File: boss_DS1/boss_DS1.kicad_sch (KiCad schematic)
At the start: 83 parts, among them J1 top_panel_connector, J2 Jack_6.35, J6 Jack_6.35, J7 Conn_01x01_Socket, J8 Conn_01x01_Socket, J9 Barrel_Jack_Switch, P1 boss_DS1_front_panel, P2 bottom_panel, Q1 MMBT5551, Q11 AO3401A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

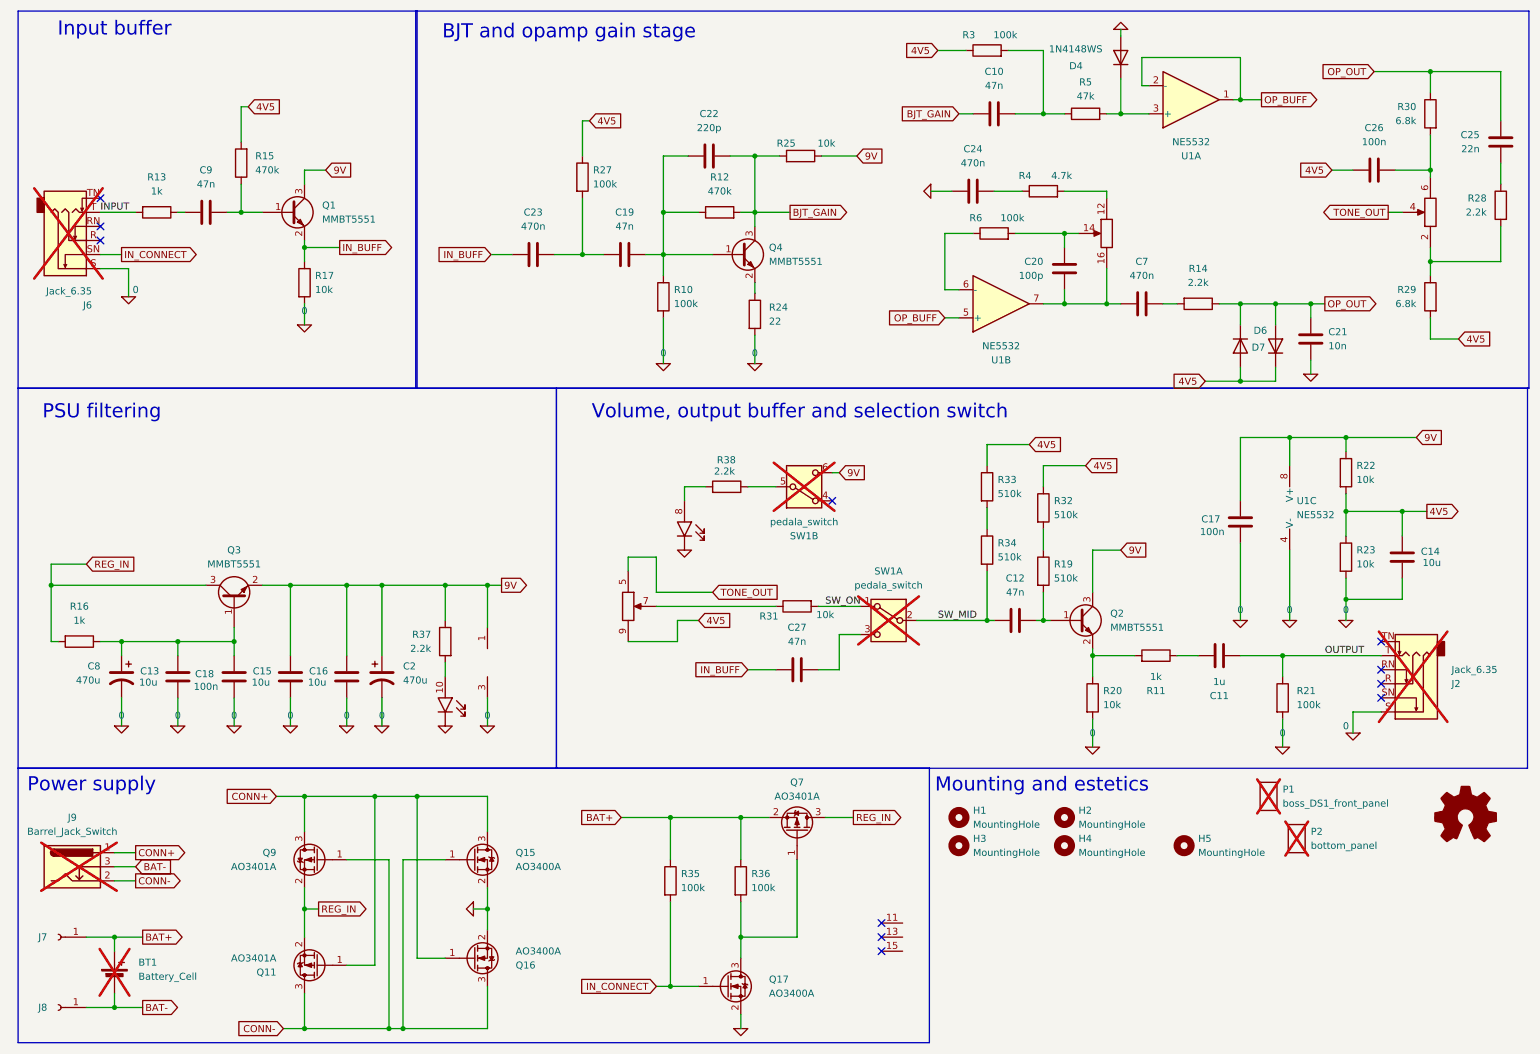
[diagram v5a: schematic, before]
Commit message: Front plate update, diodes rotated.
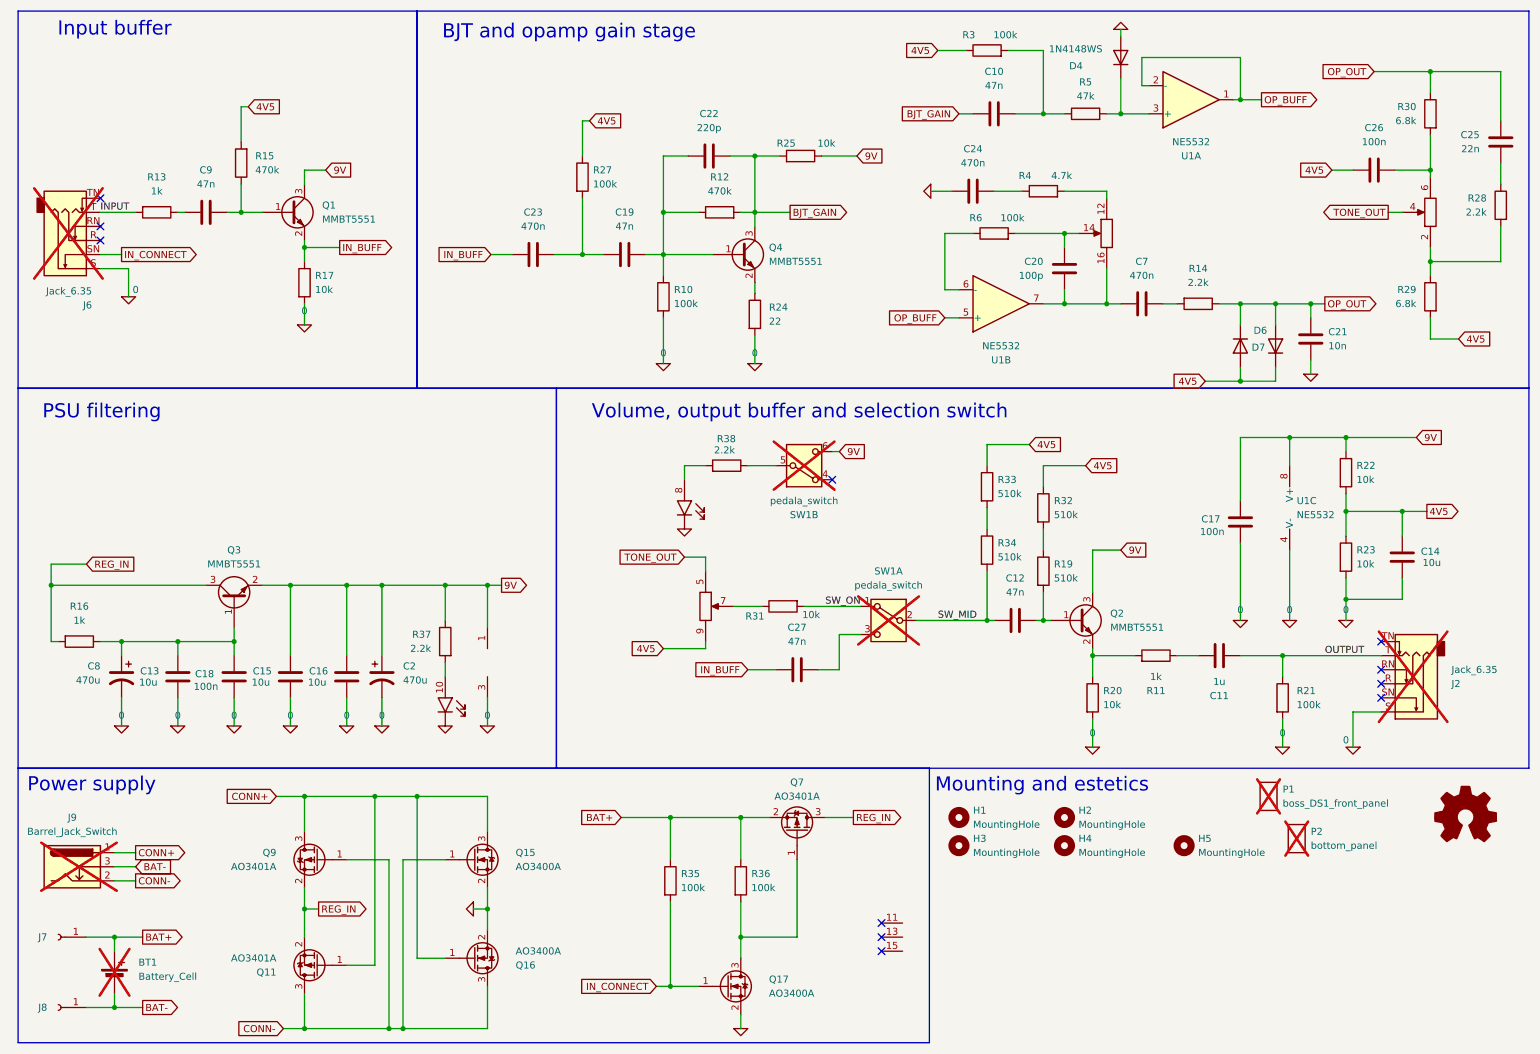
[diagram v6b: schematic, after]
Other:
- moved on the sheet: R31, R38, SW1B

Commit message: Updated all.
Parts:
- removed SIM1: Logo_Open_Hardware_Small, Symbol:OSHW-Logo2_7.3x6mm_SilkScreen, symbol Graphic:Logo_Open_Hardware_Small
- J1: footprint Connector_IDC:IDC-Header_2x08_P2.54mm_Vertical -> pedale:IDC-Header_2x08_P2.54mm_Vertical
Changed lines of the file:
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@@
 	)
 	(symbol
+		(lib_name "0_6")
 		(lib_id "Simulation_SPICE:0")
 		(at 50.8 140.97 0)
@@
 	)
 	(symbol
+		(lib_name "0_13")
 		(lib_id "Simulation_SPICE:0")
 		(at 232.41 121.92 0)
@@
 	)
 	(symbol
+		(lib_name "BC817_3")
 		(lib_id "Transistor_BJT:BC817")
 		(at 203.2 121.92 0)
@@
 	)
 	(symbol
+		(lib_name "0_12")
 		(lib_id "Simulation_SPICE:0")
 		(at 176.53 44.45 270)
@@
 			)
 		)
-		(property "Footprint" "Connector_IDC:IDC-Header_2x08_P2.54mm_Vertical"
+		(property "Footprint" "pedale:IDC-Header_2x08_P2.54mm_Vertical"
 			(at 96.52 135.89 0)
 			(effects
@@
 	)
 	(symbol
+		(lib_name "0_3")
 		(lib_id "Simulation_SPICE:0")
 		(at 210.82 15.24 0)
@@
 	)
 	(symbol
+		(lib_name "0_14")
 		(lib_id "Simulation_SPICE:0")
 		(at 40.64 140.97 0)
@@
 	)
 	(symbol
+		(lib_name "BC817_2")
 		(lib_id "Transistor_BJT:BC817")
 		(at 60.96 48.26 0)
@@
 			)
 		)
-		(property "Footprint" "Connector_IDC:IDC-Header_2x08_P2.54mm_Vertical"
+		(property "Footprint" "pedale:IDC-Header_2x08_P2.54mm_Vertical"
 			(at 266.7 48.26 0)
 			(effects
@@
 			)
 		)
-		(property "Footprint" "Connector_IDC:IDC-Header_2x08_P2.54mm_Vertical"
+		(property "Footprint" "pedale:IDC-Header_2x08_P2.54mm_Vertical"
 			(at 132.08 101.6 0)
 			(effects
@@
 			)
 		)
-		(property "Footprint" "Connector_IDC:IDC-Header_2x08_P2.54mm_Vertical"
+		(property "Footprint" "pedale:IDC-Header_2x08_P2.54mm_Vertical"
 			(at 88.9 137.16 0)
 			(effects
@@
 	)
 	(symbol
+		(lib_name "0_21")
 		(lib_id "Simulation_SPICE:0")
 		(at 252.73 144.78 0)
@@
 	)
 	(symbol
+		(lib_name "BC817_1")
 		(lib_id "Transistor_BJT:BC817")
 		(at 142.24 55.88 0)
@@
 	)
 	(symbol
-		(lib_id "Graphic:Logo_Open_Hardware_Small")
-		(at 273.05 157.48 0)
-		(unit 1)
-		(exclude_from_sim no)
-		(in_bom yes)
-		(on_board yes)
-		(dnp no)
-		(fields_autoplaced yes)
-		(property "Reference" "SIM1"
-			(at 273.05 150.495 0)
-			(effects
-				(font
-					(size 1.27 1.27)
-				)
-				(hide yes)
-			)
-		)
-		(property "Value" "Logo_Open_Hardware_Small"
-			(at 273.05 163.195 0)
-			(effects
-				(font
-					(size 1.27 1.27)
-				)
-				(hide yes)
-			)
-		)
-		(property "Footprint" "Symbol:OSHW-Logo2_7.3x6mm_SilkScreen"
-			(at 273.05 157.48 0)
-			(effects
-				(font
-					(size 1.27 1.27)
-				)
-				(hide yes)
-			)
-		)
-		(property "Datasheet" "~"
-			(at 273.05 157.48 0)
-			(effects
-				(font
-					(size 1.27 1.27)
-				)
-				(hide yes)
-			)
-		)
-		(property "Description" "Open Hardware logo, small"
-			(at 273.05 157.48 0)
-			(effects
-				(font
-					(size 1.27 1.27)
-				)
-				(hide yes)
-			)
-		)
-		(instances
-			(project "tube_screamer"
-				(path "/e0801131-6974-42d8-8070-4ed960891aa7"
-					(reference "SIM1")
-					(unit 1)
-				)
-			)
-		)
-	)
-	(symbol
+		(lib_name "0_11")
 		(lib_id "Simulation_SPICE:0")
 		(at 63.5 68.58 0)
@@
 			)
 		)
-		(property "Footprint" "Connector_IDC:IDC-Header_2x08_P2.54mm_Vertical"
+		(property "Footprint" "pedale:IDC-Header_2x08_P2.54mm_Vertical"
 			(at 208.28 52.07 0)
 			(effects
@@
 	)
 	(symbol
+		(lib_name "MountingHole_1")
 		(lib_id "Mechanical:MountingHole")
 		(at 222.25 162.56 0)
@@
 	)
 	(symbol
+		(lib_name "MountingHole_4")
 		(lib_id "Mechanical:MountingHole")
 		(at 200.66 157.48 0)
@@
 	)
 	(symbol
+		(lib_name "0_1")
 		(lib_id "Simulation_SPICE:0")
 		(at 77.47 140.97 0)
@@
 	)
 	(symbol
+		(lib_name "0_19")
 		(lib_id "Simulation_SPICE:0")
 		(at 71.12 140.97 0)
@@
 	)
 	(symbol
+		(lib_name "0_15")
 		(lib_id "Simulation_SPICE:0")
 		(at 245.11 77.47 0)
@@
 	)
 	(symbol
+		(lib_name "0_18")
 		(lib_id "Simulation_SPICE:0")
 		(at 240.03 144.78 0)
@@
 	)
 	(symbol
+		(lib_name "MountingHole_3")
 		(lib_id "Mechanical:MountingHole")
 		(at 181.61 157.48 0)
@@
 	)
 	(symbol
+		(lib_name "0_5")
 		(lib_id "Simulation_SPICE:0")
 		(at 128.27 75.565 0)
@@
 	)
 	(symbol
+		(lib_name "0_9")
 		(lib_id "Simulation_SPICE:0")
 		(at 30.48 140.97 0)
@@
 	)
 	(symbol
+		(lib_name "0_16")
 		(lib_id "Simulation_SPICE:0")
 		(at 93.98 173.99 270)
@@
 	)
 	(symbol
+		(lib_name "0_7")
 		(lib_id "Simulation_SPICE:0")
 		(at 142.24 195.58 0)
@@
 	)
 	(symbol
+		(lib_name "MountingHole_2")
 		(lib_id "Mechanical:MountingHole")
 		(at 200.66 162.56 0)
@@
 	)
 	(symbol
+		(lib_name "0_8")
 		(lib_id "Simulation_SPICE:0")
 		(at 251.46 121.92 0)
@@
 			)
 		)
-		(property "Footprint" "Connector_IDC:IDC-Header_2x08_P2.54mm_Vertical"
+		(property "Footprint" "pedale:IDC-Header_2x08_P2.54mm_Vertical"
 			(at 135.89 119.38 0)
 			(effects
@@
 	)
 	(symbol
+		(lib_name "0_2")
 		(lib_id "Simulation_SPICE:0")
 		(at 144.78 75.565 0)
@@
 	)
 	(symbol
+		(lib_name "0_17")
 		(lib_id "Simulation_SPICE:0")
 		(at 241.3 121.92 0)
@@
 	)
 	(symbol
+		(lib_name "0_4")
 		(lib_id "Simulation_SPICE:0")
 		(at 60.96 140.97 0)
@@
 	)
 	(symbol
+		(lib_name "0_20")
 		(lib_id "Simulation_SPICE:0")
 		(at 205.74 144.78 0)
@@
 	)
 	(symbol
+		(lib_name "0_10")
 		(lib_id "Simulation_SPICE:0")
 		(at 31.75 63.5 0)
@@
 			)
 		)
-		(property "Footprint" "Connector_IDC:IDC-Header_2x08_P2.54mm_Vertical"
+		(property "Footprint" "pedale:IDC-Header_2x08_P2.54mm_Vertical"
 			(at 167.64 181.61 0)
 			(effects
